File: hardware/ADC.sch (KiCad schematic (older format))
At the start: 12 parts, among them J4 691327310016, J5 691327310016, U1 ADS8586S

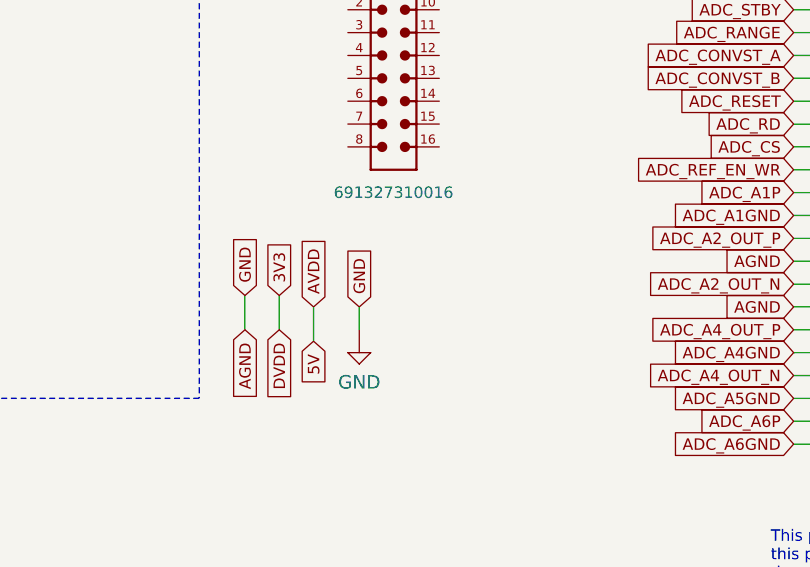
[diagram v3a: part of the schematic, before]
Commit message: Before AGND - GND
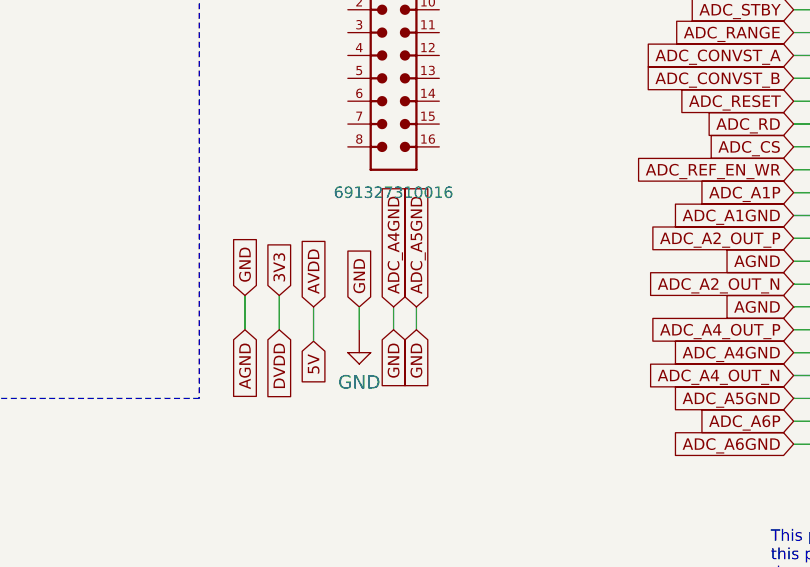
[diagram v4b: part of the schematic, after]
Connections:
- net ADC_A5GND is gone; now on net ADC_A4GND: U1.60 (AIN_5GND)
- net ADC_REFGND is gone; now on net ADC_A4GND: C26.2, C27.1, C28.1, C29.2, C33.2, C34.2, C35.2, C38.2, C39.2, J4.12, J4.9, U1.2 (AGND), U1.26 (AGND), U1.35 (AGND), U1.40 (AGND), U1.41 (AGND), U1.43 (REFGND), U1.46 (REFGND), U1.52 (AIN_2GND), U1.54 (AIN_3GND), U1.55 (AGND), U1.56 (AGND), U1.63 (AGND), U1.64 (AGND)
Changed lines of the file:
@@
 P 4600 1650
 AR Path="/5E22C01C/5E41D834" Ref="#SUPPLY?"  Part="1"
-AR Path="/5E22D897/5E41D834" Ref="#SUPPLY?"  Part="1"
-F 0 "#SUPPLY?" H 4600 1650 50  0001 C CNN
+AR Path="/5E22D897/5E41D834" Ref="#SUPPLY0116"  Part="1"
+F 0 "#SUPPLY0116" H 4600 1650 50  0001 C CNN
 F 1 "GND" V 4600 1572 59  0000 R CNN
 F 2 "" H 4600 1650 50  0001 C CNN
@@
 Wire Wire Line
 	4600 1450 5200 1450
+Text GLabel 3350 3650 1    50   Input ~ 0
+ADC_A4GND
+Text GLabel 3350 3750 3    50   Input ~ 0
+GND
+Text GLabel 3450 3650 1    50   Input ~ 0
+ADC_A5GND
+Wire Wire Line
+	3350 3750 3350 3650
+Text GLabel 3450 3750 3    50   Input ~ 0
+GND
+Wire Wire Line
+	3450 3750 3450 3650
 $EndSCHEMATC

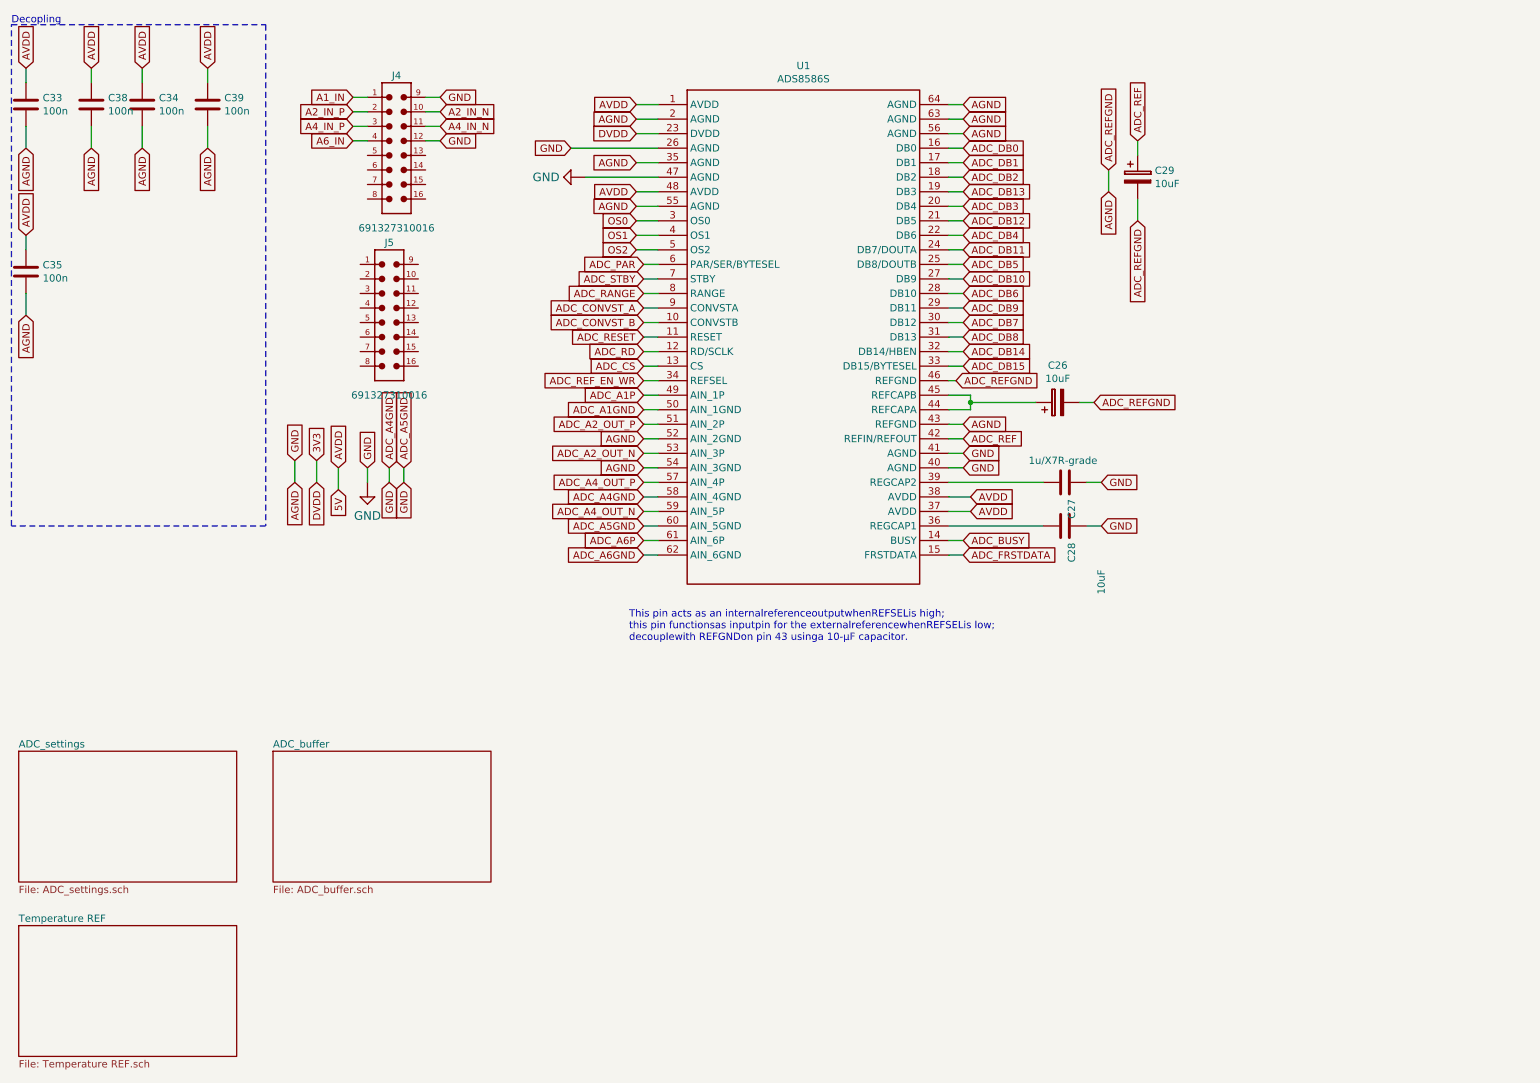
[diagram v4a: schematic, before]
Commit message: Finishing routing
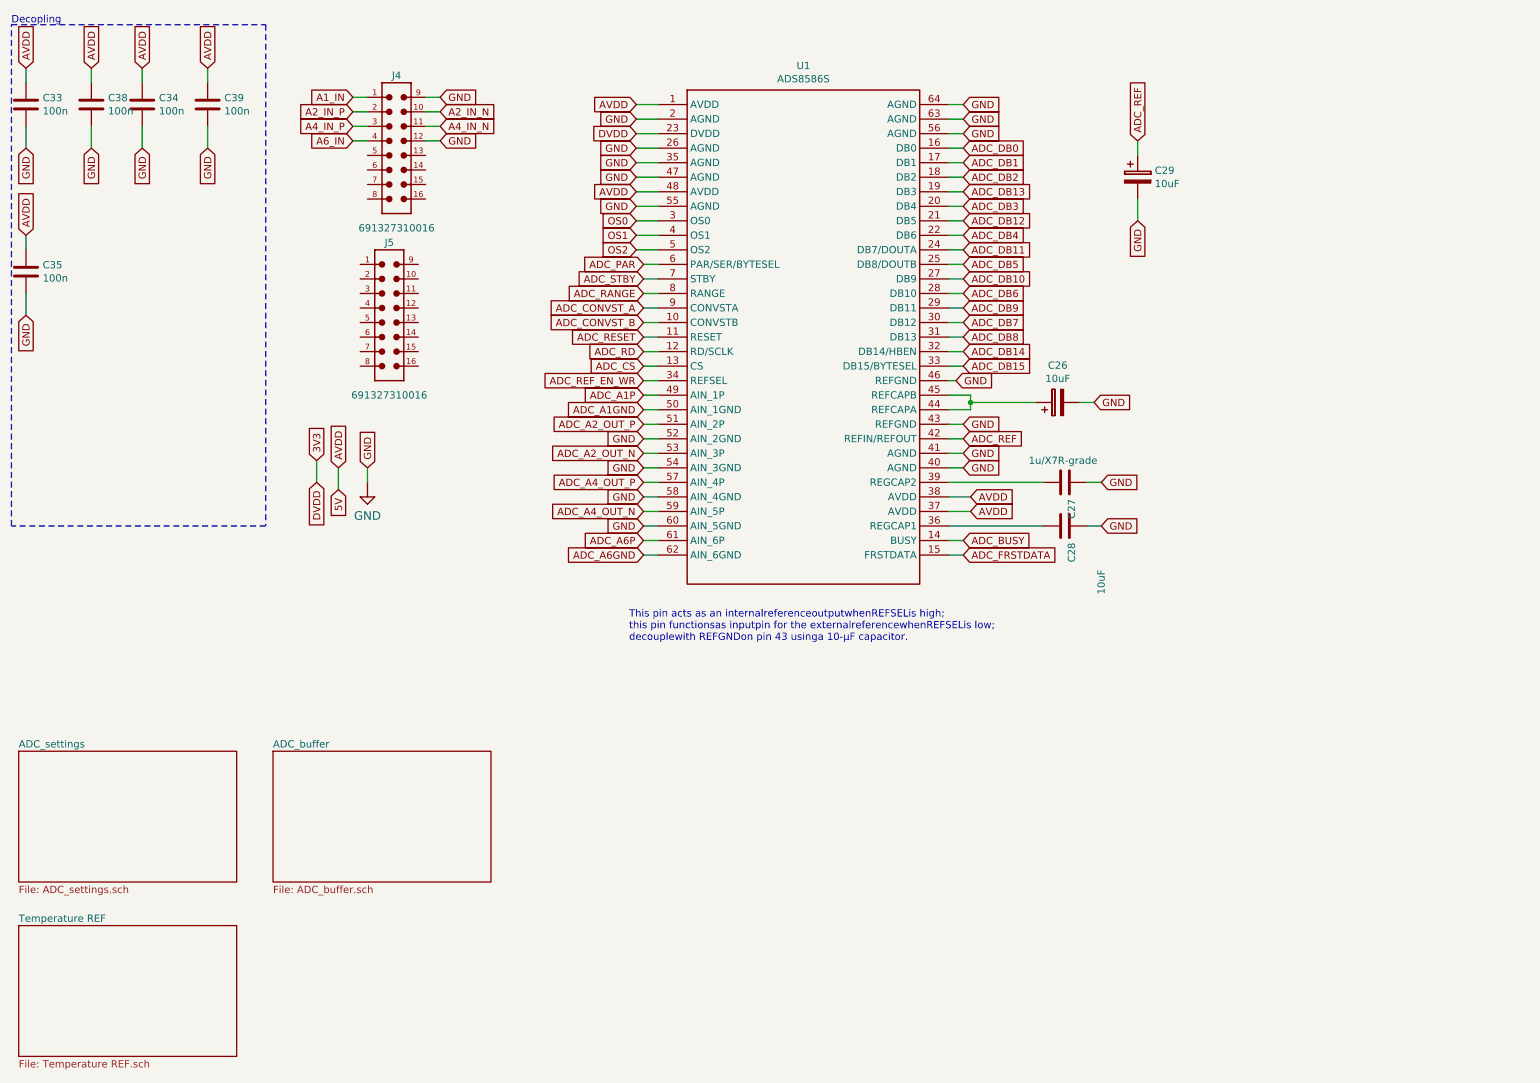
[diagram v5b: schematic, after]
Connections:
- net ADC_A4GND is gone; now on net GND: C26.2, C27.1, C28.1, C29.2, C33.2, C34.2, C35.2, C38.2, C39.2, J4.12, J4.9, U1.2 (AGND), U1.26 (AGND), U1.35 (AGND), U1.40 (AGND), U1.41 (AGND), U1.43 (REFGND), U1.46 (REFGND), U1.52 (AIN_2GND), U1.54 (AIN_3GND), U1.55 (AGND), U1.56 (AGND), U1.58 (AIN_4GND), U1.60 (AIN_5GND), U1.63 (AGND), U1.64 (AGND)
- net GND: now reaches U1.47 (AGND)
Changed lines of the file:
@@
 AVDD
 Text GLabel 850  1450 3    50   Input ~ 0
-AGND
+GND
 $Comp
 L antena:C C33
@@
 AVDD
 Text GLabel 1300 1450 3    50   Input ~ 0
-AGND
+GND
 $Comp
 L antena:C C38
@@
 AVDD
 Text GLabel 1650 1450 3    50   Input ~ 0
-AGND
+GND
 $Comp
 L antena:C C34
@@
 AVDD
 Text GLabel 2100 1450 3    50   Input ~ 0
-AGND
+GND
 $Comp
 L antena:C C39
@@
 AVDD
 Text GLabel 850  2600 3    50   Input ~ 0
-AGND
+GND
 $Comp
 L antena:C C35
@@
 Wire Wire Line
 	3100 1300 3200 1300
-Text GLabel 2700 3750 3    50   Input ~ 0
-AGND
-Text GLabel 2700 3600 1    50   Input ~ 0
-GND
-Wire Wire Line
-	2700 3600 2700 3750
 Text GLabel 2850 3750 3    50   Input ~ 0
 DVDD
@@
 	5100 3750 5200 3750
 Wire Wire Line
-	5100 3850 5200 3850
-Wire Wire Line
 	5100 3950 5200 3950
 Wire Wire Line
-	5100 4050 5200 4050
-Wire Wire Line
 	5100 4150 5200 4150
-Wire Wire Line
-	5100 4250 5200 4250
 Wire Wire Line
 	5100 3050 5200 3050
@@
 	7200 4250 7300 4250
 Text GLabel 8500 1950 3    50   Input ~ 0
-ADC_REFGND
+GND
 Text GLabel 7300 3450 2    50   Input ~ 0
 ADC_REF
@@
 $EndComp
 Text GLabel 7250 3050 2    50   Input ~ 0
-ADC_REFGND
+GND
 Wire Wire Line
 	7200 3050 7250 3050
@@
 	7350 3200 7350 3250
 Text GLabel 8200 3200 2    50   Input ~ 0
-ADC_REFGND
+GND
 Wire Wire Line
 	8100 3200 8200 3200
-Text GLabel 8300 1600 1    50   Input ~ 0
-ADC_REFGND
 Text GLabel 7300 3550 2    50   Input ~ 0
 GND
@@
 	5050 1150 5200 1150
 Text GLabel 5050 1250 0    50   Input ~ 0
-AGND
+GND
 Text GLabel 5050 1550 0    50   Input ~ 0
-AGND
+GND
 Text GLabel 5050 1850 0    50   Input ~ 0
-AGND
+GND
 Text GLabel 7300 1150 2    50   Input ~ 0
-AGND
+GND
 Text GLabel 7300 1250 2    50   Input ~ 0
-AGND
+GND
 Text GLabel 7300 1350 2    50   Input ~ 0
-AGND
+GND
 Text GLabel 5100 3250 0    50   Input ~ 0
 ADC_A1GND
-Text GLabel 5100 3850 0    50   Input ~ 0
-ADC_A4GND
-Text GLabel 5100 4050 0    50   Input ~ 0
-ADC_A5GND
-Text GLabel 5100 4250 0    50   Input ~ 0
-ADC_A6GND
 Text GLabel 5100 3650 0    50   Input ~ 0
-AGND
+GND
 Text GLabel 5100 3450 0    50   Input ~ 0
-AGND
+GND
 Text GLabel 7300 3350 2    50   Input ~ 0
-AGND
-Text GLabel 8300 1750 3    50   Input ~ 0
-AGND
-Wire Wire Line
-	8300 1600 8300 1750
+GND
 $Comp
 L EEZ_DIB_MCU_r1B1-eagle-import:GND #SUPPLY?
@@
 Wire Wire Line
 	3200 3650 3200 3750
-$Comp
-L EEZ_DIB_MCU_r1B1-eagle-import:GND #SUPPLY?
-U 1 1 5E41D834
-P 4600 1650
-AR Path="/5E22C01C/5E41D834" Ref="#SUPPLY?"  Part="1"
-AR Path="/5E22D897/5E41D834" Ref="#SUPPLY0116"  Part="1"
-F 0 "#SUPPLY0116" H 4600 1650 50  0001 C CNN
-F 1 "GND" V 4600 1572 59  0000 R CNN
-F 2 "" H 4600 1650 50  0001 C CNN
-F 3 "" H 4600 1650 50  0001 C CNN
-	1    4600 1650
-	0    1    1    0
-$EndComp
-Wire Wire Line
-	4700 1650 5200 1650
-Text GLabel 4600 1450 0    50   Input ~ 0
-GND
-Wire Wire Line
-	4600 1450 5200 1450
-Text GLabel 3350 3650 1    50   Input ~ 0
-ADC_A4GND
-Text GLabel 3350 3750 3    50   Input ~ 0
-GND
-Text GLabel 3450 3650 1    50   Input ~ 0
-ADC_A5GND
-Wire Wire Line
-	3350 3750 3350 3650
-Text GLabel 3450 3750 3    50   Input ~ 0
-GND
-Wire Wire Line
-	3450 3750 3450 3650
+Text GLabel 5050 1450 0    50   Input ~ 0
+GND
+Wire Wire Line
+	5050 1450 5200 1450
+Text GLabel 5050 1650 0    50   Input ~ 0
+GND
+Wire Wire Line
+	5200 1650 5050 1650
+Wire Wire Line
+	5100 4050 5200 4050
+Wire Wire Line
+	5100 4250 5200 4250
+Text GLabel 5100 4250 0    50   Input ~ 0
+ADC_A6GND
+Wire Wire Line
+	5100 3850 5200 3850
+Text GLabel 5100 3850 0    50   Input ~ 0
+GND
+Text GLabel 5100 4050 0    50   Input ~ 0
+GND
 $EndSCHEMATC

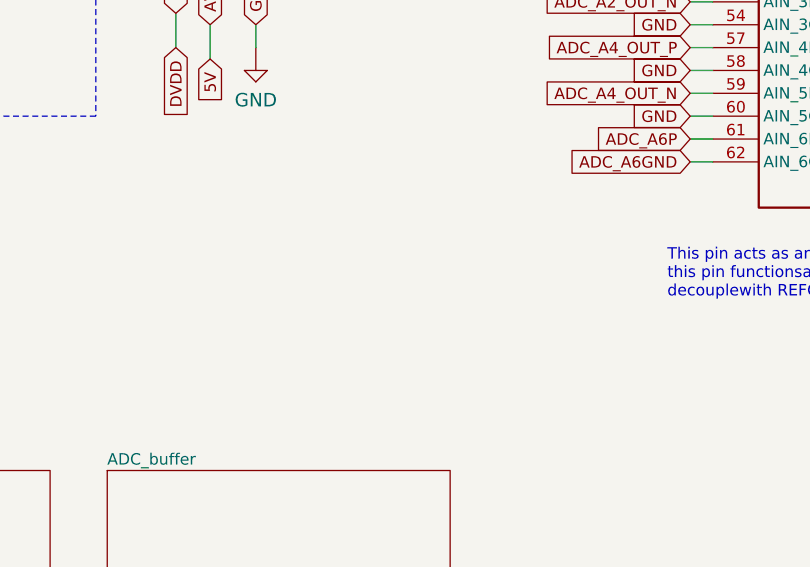
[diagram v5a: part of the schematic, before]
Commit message: Adding pcb changes to PBC
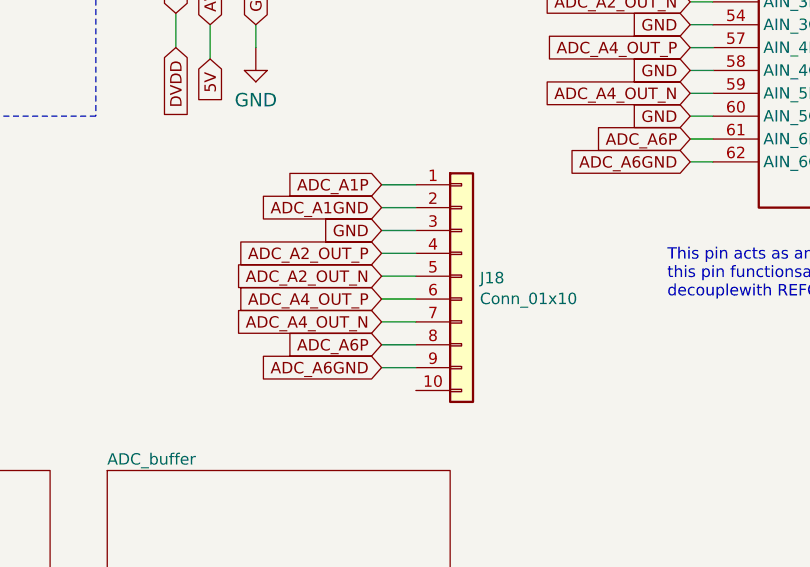
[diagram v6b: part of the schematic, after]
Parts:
- added J18: Conn_01x10, Connector_PinHeader_1.00mm:PinHeader_1x10_P1.00mm_Vertical, symbol Connector_Generic:Conn_01x10
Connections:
- net ADC_A1GND: now also J18.2 (Pin_2)
- net ADC_A1P: now also J18.1 (Pin_1)
- net ADC_A2_OUT_N: now also J18.5 (Pin_5)
- net ADC_A2_OUT_P: now also J18.4 (Pin_4)
- net ADC_A4_OUT_N: now also J18.7 (Pin_7)
- net ADC_A4_OUT_P: now also J18.6 (Pin_6)
- net ADC_A6GND: now also J18.9 (Pin_9)
- net ADC_A6P: now also J18.8 (Pin_8)
- net GND: now also J18.3 (Pin_3)
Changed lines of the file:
@@
 Text GLabel 5100 4050 0    50   Input ~ 0
 GND
+Text GLabel 3750 4350 0    50   Input ~ 0
+ADC_A1P
+Text GLabel 3750 4650 0    50   Input ~ 0
+ADC_A2_OUT_P
+Text GLabel 3750 4450 0    50   Input ~ 0
+ADC_A1GND
+Text GLabel 3750 4550 0    50   Input ~ 0
+GND
+Text GLabel 3750 4750 0    50   Input ~ 0
+ADC_A2_OUT_N
+Text GLabel 3750 4850 0    50   Input ~ 0
+ADC_A4_OUT_P
+Text GLabel 3750 4950 0    50   Input ~ 0
+ADC_A4_OUT_N
+Text GLabel 3750 5050 0    50   Input ~ 0
+ADC_A6P
+Text GLabel 3750 5150 0    50   Input ~ 0
+ADC_A6GND
+$Comp
+L Connector_Generic:Conn_01x10 J18
+U 1 1 5E48F401
+P 4100 4750
+F 0 "J18" H 4180 4742 50  0000 L CNN
+F 1 "Conn_01x10" H 4180 4651 50  0000 L CNN
+F 2 "Connector_PinHeader_1.00mm:PinHeader_1x10_P1.00mm_Vertical" H 4100 4750 50  0001 C CNN
+F 3 "~" H 4100 4750 50  0001 C CNN
+	1    4100 4750
+	1    0    0    -1
+$EndComp
+Wire Wire Line
+	3750 4350 3900 4350
+Wire Wire Line
+	3750 4450 3900 4450
+Wire Wire Line
+	3750 4550 3900 4550
+Wire Wire Line
+	3750 4650 3900 4650
+Wire Wire Line
+	3750 4750 3900 4750
+Wire Wire Line
+	3750 4850 3900 4850
+Wire Wire Line
+	3750 4950 3900 4950
+Wire Wire Line
+	3750 5050 3900 5050
+Wire Wire Line
+	3750 5150 3900 5150
 $EndSCHEMATC
